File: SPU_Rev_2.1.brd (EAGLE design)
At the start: 127.6 x 101.6 mm, 257 parts, among them Q1 12MHz

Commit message: added LWL IN
added LWL IN
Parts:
- removed C63: 10u, rcl:E/7260-38W
- added C78: (no value), rcl:C1206
- added U$9: PLR135, everlight-fiber-optics-spdif:PLR135-T1
- moved C65 7.11 mm to (91.2, 22.7), turned to 0 degrees
- moved C36 4.72 mm to (100.6, 9.78)
- moved C39 4.57 mm to (91.2, 30.6)
- moved C64 4.45 mm to (91.2, 30.7)
- moved U$8 1.02 mm to (62.0, 16.1)
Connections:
- new net LWL_IN: U$9.VOUT, U_STM32F779.7
- net 3V3: now also C78.1, U$9.VCC
- net 5V: no longer C63.+
- net GND: now also C78.2, U$9.GND; no longer C63.-
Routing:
- net LWL_IN: track 0.00 -> 51.8 mm, vias 0 -> 1
- net 3V3: track 887.6 -> 917.4 mm
- net GND: track 1457.2 -> 1427.5 mm, vias 169 -> 168
- net 5V: track 193.2 -> 197.8 mm
- net 28V: track 219.9 -> 223.9 mm, vias 11 -> 13
- net LWL_OUT: track 37.8 -> 39.0 mm
- net LED_4: track 81.3 -> 82.1 mm

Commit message: Added PT100 ADC R/C values
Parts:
- C_ICM1_PT3, C_ICM2_PT3: value (none) -> 4n7
- C_IDIFF_PT3: value (none) -> 47n
- C_RDIFF_PT3: value (none) -> 100n
- R_I1_PT3, R_I2_PT3: value (none) -> 5k
- R_R1_PT3: value (none) -> 3k16
- R_R2_PT3: value (none) -> inf
- R_REF_PT3: value (none) -> 1k62
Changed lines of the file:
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@@
 <drawing>
 <settings>
-<setting alwaysvectorfont="no"/>
+<setting alwaysvectorfont="yes"/>
 <setting verticaltext="up"/>
 </settings>
@@
 <attribute name="VALUE" x="22.8242" y="84.5312" size="1.016" layer="27" ratio="10" rot="R90"/>
 </element>
-<element name="R_REF_PT3" library="++Bedrahtet" package="R0603" value="" x="25.146" y="87.884" smashed="yes" rot="MR270">
+<element name="R_REF_PT3" library="++Bedrahtet" package="R0603" value="1k62" x="25.146" y="87.884" smashed="yes" rot="MR270">
 <attribute name="NAME" x="30.48" y="89.789" size="1.016" layer="26" font="vector" ratio="15" rot="MR0"/>
 <attribute name="VALUE" x="27.178" y="88.773" size="1.27" layer="28" rot="MR270"/>
 </element>
-<element name="R_R1_PT3" library="++Bedrahtet" package="R0603" value="" x="22.987" y="87.884" smashed="yes" rot="MR270">
+<element name="R_R1_PT3" library="++Bedrahtet" package="R0603" value="3k16" x="22.987" y="87.884" smashed="yes" rot="MR270">
 <attribute name="NAME" x="28.067" y="91.186" size="1.016" layer="26" font="vector" ratio="15" rot="MR0"/>
 <attribute name="VALUE" x="25.019" y="88.773" size="1.27" layer="28" rot="MR270"/>
 </element>
-<element name="R_R2_PT3" library="++Bedrahtet" package="R0603" value="" x="17.272" y="80.264" smashed="yes" rot="MR270">
+<element name="R_R2_PT3" library="++Bedrahtet" package="R0603" value="inf" x="17.272" y="80.264" smashed="yes" rot="MR270">
 <attribute name="NAME" x="16.129" y="81.915" size="1.016" layer="26" font="vector" ratio="15" rot="MR270"/>
 <attribute name="VALUE" x="19.304" y="81.153" size="1.27" layer="28" rot="MR270"/>
 </element>
-<element name="C_RDIFF_PT3" library="rcl" library_urn="urn:adsk.eagle:library:334" package="C0603" package3d_urn="urn:adsk.eagle:package:23616/2" value="" x="17.653" y="86.106" smashed="yes" rot="MR0">
+<element name="C_RDIFF_PT3" library="rcl" library_urn="urn:adsk.eagle:library:334" package="C0603" package3d_urn="urn:adsk.eagle:package:23616/2" value="100n" x="17.653" y="86.106" smashed="yes" rot="MR0">
 <attribute name="NAME" x="14.478" y="88.265" size="1.016" layer="26" font="vector" ratio="15" rot="MR270"/>
 <attribute name="SPICEPREFIX" value="C" x="26.416" y="95.504" size="1.778" layer="28" rot="MR0" display="off"/>
@@
 <attribute name="VALUE" x="15.367" y="80.645" size="1.27" layer="27" rot="R270"/>
 </element>
-<element name="R_I1_PT3" library="++Bedrahtet" package="R0603" value="" x="22.987" y="81.28" smashed="yes" rot="R180">
+<element name="R_I1_PT3" library="++Bedrahtet" package="R0603" value="5k" x="22.987" y="81.28" smashed="yes" rot="R180">
 <attribute name="NAME" x="28.956" y="79.502" size="1.016" layer="25" font="vector" ratio="15" rot="R180"/>
 <attribute name="VALUE" x="23.876" y="83.312" size="1.27" layer="27" rot="R180"/>
 </element>
-<element name="R_I2_PT3" library="++Bedrahtet" package="R0603" value="" x="22.987" y="89.154" smashed="yes" rot="R90">
+<element name="R_I2_PT3" library="++Bedrahtet" package="R0603" value="5k" x="22.987" y="89.154" smashed="yes" rot="R90">
 <attribute name="NAME" x="23.876" y="88.9" size="0.8128" layer="25" font="vector" ratio="15"/>
 <attribute name="VALUE" x="25.019" y="88.265" size="1.27" layer="27" rot="R90"/>
 </element>
-<element name="C_IDIFF_PT3" library="rcl" library_urn="urn:adsk.eagle:library:334" package="C0603" package3d_urn="urn:adsk.eagle:package:23616/2" value="" x="24.003" y="84.328" smashed="yes" rot="R180">
+<element name="C_IDIFF_PT3" library="rcl" library_urn="urn:adsk.eagle:library:334" package="C0603" package3d_urn="urn:adsk.eagle:package:23616/2" value="47n" x="24.003" y="84.328" smashed="yes" rot="R180">
 <attribute name="NAME" x="24.638" y="83.185" size="0.8128" layer="25" font="vector" ratio="15" rot="R180"/>
 <attribute name="SPICEPREFIX" value="C" x="24.003" y="85.852" size="1.778" layer="27" rot="R180" display="off"/>
 <attribute name="VALUE" x="24.638" y="86.233" size="1.27" layer="27" rot="R180"/>
 </element>
-<element name="C_ICM1_PT3" library="rcl" library_urn="urn:adsk.eagle:library:334" package="C0603" package3d_urn="urn:adsk.eagle:package:23616/2" value="" x="20.828" y="80.899" smashed="yes" rot="MR270">
+<element name="C_ICM1_PT3" library="rcl" library_urn="urn:adsk.eagle:library:334" package="C0603" package3d_urn="urn:adsk.eagle:package:23616/2" value="4n7" x="20.828" y="80.899" smashed="yes" rot="MR270">
 <attribute name="NAME" x="19.558" y="82.677" size="1.016" layer="26" font="vector" ratio="15" rot="MR270"/>
 <attribute name="SPICEPREFIX" value="C" x="25.908" y="92.456" size="1.778" layer="28" rot="MR270" display="off"/>
 <attribute name="VALUE" x="22.733" y="81.534" size="1.27" layer="28" rot="MR270"/>
 </element>
-<element name="C_ICM2_PT3" library="rcl" library_urn="urn:adsk.eagle:library:334" package="C0603" package3d_urn="urn:adsk.eagle:package:23616/2" value="" x="24.003" y="86.487" smashed="yes" rot="R180">
+<element name="C_ICM2_PT3" library="rcl" library_urn="urn:adsk.eagle:library:334" package="C0603" package3d_urn="urn:adsk.eagle:package:23616/2" value="4n7" x="24.003" y="86.487" smashed="yes" rot="R180">
 <attribute name="SPICEPREFIX" value="C" x="24.003" y="91.567" size="1.778" layer="27" rot="R180" display="off"/>
 <attribute name="VALUE" x="24.638" y="88.392" size="1.27" layer="27" rot="R180"/>

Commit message: RS422 confirmed
RS422 driver functionality plus optocouplers tested and confirmed
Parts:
- JP_MS, X_PROG: value (none) -> x
- LED7, LED8: value (none) -> 1V9
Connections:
- net PRD_ON renamed PDR_ON
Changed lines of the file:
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@@
 <drawing>
 <settings>
-<setting alwaysvectorfont="yes"/>
+<setting alwaysvectorfont="no"/>
 <setting verticaltext="up"/>
 </settings>
@@
 <attribute name="VALUE" x="66.548" y="12.954" size="1.27" layer="28" rot="MR90"/>
 </element>
-<element name="LED7" library="adafruit" library_urn="urn:adsk.eagle:library:420" package="CHIP-LED0805" package3d_urn="urn:adsk.eagle:package:6240557/1" value="" x="83.439" y="8.255" smashed="yes" rot="R180">
+<element name="LED7" library="adafruit" library_urn="urn:adsk.eagle:library:420" package="CHIP-LED0805" package3d_urn="urn:adsk.eagle:package:6240557/1" value="1V9" x="83.439" y="8.255" smashed="yes" rot="R180">
 <attribute name="NAME" x="83.947" y="9.779" size="1.016" layer="26" font="vector" ratio="15" rot="MR270"/>
 <attribute name="VALUE" x="80.899" y="9.525" size="1.27" layer="27" rot="R270"/>
@@
 <attribute name="VALUE" x="81.026" y="12.954" size="1.27" layer="28" rot="MR90"/>
 </element>
-<element name="LED8" library="adafruit" library_urn="urn:adsk.eagle:library:420" package="CHIP-LED0805" package3d_urn="urn:adsk.eagle:package:6240557/1" value="" x="81.407" y="8.255" smashed="yes" rot="R180">
+<element name="LED8" library="adafruit" library_urn="urn:adsk.eagle:library:420" package="CHIP-LED0805" package3d_urn="urn:adsk.eagle:package:6240557/1" value="1V9" x="81.407" y="8.255" smashed="yes" rot="R180">
 <attribute name="NAME" x="81.915" y="9.779" size="1.016" layer="26" font="vector" ratio="15" rot="MR270"/>
 <attribute name="VALUE" x="78.867" y="9.525" size="1.27" layer="27" rot="R270"/>
@@
 <attribute name="VALUE" x="59.315184375" y="62.405990625" size="1.27" layer="28" rot="MR270"/>
 </element>
-<element name="JP_MS" library="aSparkFun" package="1X02" value="" x="50.504346875" y="65.166596875" smashed="yes" rot="R90">
+<element name="JP_MS" library="aSparkFun" package="1X02" value="x" x="50.504346875" y="65.166596875" smashed="yes" rot="R90">
 <attribute name="NAME" x="47.844453125" y="69.402603125" size="1.016" layer="25" font="vector" ratio="15" rot="R270"/>
 <attribute name="VALUE" x="53.679346875" y="63.896596875" size="1.27" layer="27" rot="R90"/>
@@
 <attribute name="VALUE" x="115.323" y="72.821" size="1.27" layer="28" rot="SMR90"/>
 </element>
-<element name="X_PROG" library="con-lstb" library_urn="urn:adsk.eagle:library:162" package="MA10-2" package3d_urn="urn:adsk.eagle:package:8331/1" value="" x="72.771" y="42.037" smashed="yes" rot="R180">
+<element name="X_PROG" library="con-lstb" library_urn="urn:adsk.eagle:library:162" package="MA10-2" package3d_urn="urn:adsk.eagle:package:8331/1" value="x" x="72.771" y="42.037" smashed="yes" rot="R180">
 <attribute name="MF" value="" x="72.771" y="42.037" size="1.27" layer="27" font="vector" ratio="12" rot="R180" display="off"/>
 <attribute name="MPN" value="" x="72.771" y="42.037" size="1.27" layer="27" font="vector" ratio="12" rot="R180" display="off"/>
@@
 <wire x1="61.989553125" y1="81.90501875" x2="61.951396875" y2="81.943175" width="0.254" layer="1"/>
 </signal>
-<signal name="PRD_ON">
+<signal name="PDR_ON">
 <contactref element="U_STM32F779" pad="203"/>
 <contactref element="R9" pad="1"/>

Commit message: Opto Pull-up adjusted
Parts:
- C77, C78: value (none) -> 100n
- RN12: value 300 -> 1k
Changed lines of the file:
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@@
 <attribute name="VALUE" x="108.204" y="87.605" size="1.27" layer="27" align="top-center"/>
 </element>
-<element name="RN12" library="resistor-dil" library_urn="urn:adsk.eagle:library:342" package="EXBS8V" package3d_urn="urn:adsk.eagle:package:24925/1" value="300" x="108.077" y="87.122" smashed="yes" rot="MR90">
+<element name="RN12" library="resistor-dil" library_urn="urn:adsk.eagle:library:342" package="EXBS8V" package3d_urn="urn:adsk.eagle:package:24925/1" value="1k" x="108.077" y="87.122" smashed="yes" rot="MR90">
 <attribute name="MF" value="" x="108.077" y="87.122" size="1.778" layer="28" rot="MR90" display="off"/>
 <attribute name="MPN" value="" x="108.077" y="87.122" size="1.778" layer="28" rot="MR90" display="off"/>
@@
 <attribute name="NAME" x="61.722" y="9.652" size="1.778" layer="26" rot="MR90"/>
 </element>
-<element name="C77" library="rcl" library_urn="urn:adsk.eagle:library:334" package="C1206" package3d_urn="urn:adsk.eagle:package:23618/2" value="" x="57.658" y="19.685" smashed="yes" rot="MR0">
+<element name="C77" library="rcl" library_urn="urn:adsk.eagle:library:334" package="C1206" package3d_urn="urn:adsk.eagle:package:23618/2" value="100n" x="57.658" y="19.685" smashed="yes" rot="MR0">
 <attribute name="NAME" x="59.182" y="21.082" size="1.27" layer="26" rot="MR0"/>
 <attribute name="SPICEPREFIX" value="C" x="57.658" y="19.685" size="1.778" layer="28" rot="MR0" display="off"/>
@@
 <attribute name="NAME" x="94.996" y="14.351" size="1.778" layer="26" rot="MR90"/>
 </element>
-<element name="C78" library="rcl" library_urn="urn:adsk.eagle:library:334" package="C1206" package3d_urn="urn:adsk.eagle:package:23618/2" value="" x="91.059" y="11.938" smashed="yes" rot="MR270">
+<element name="C78" library="rcl" library_urn="urn:adsk.eagle:library:334" package="C1206" package3d_urn="urn:adsk.eagle:package:23618/2" value="100n" x="91.059" y="11.938" smashed="yes" rot="MR270">
 <attribute name="NAME" x="89.789" y="13.208" size="1.27" layer="26" rot="MR270"/>
 <attribute name="SPICEPREFIX" value="C" x="91.059" y="11.938" size="1.778" layer="28" rot="MR270" display="off"/>

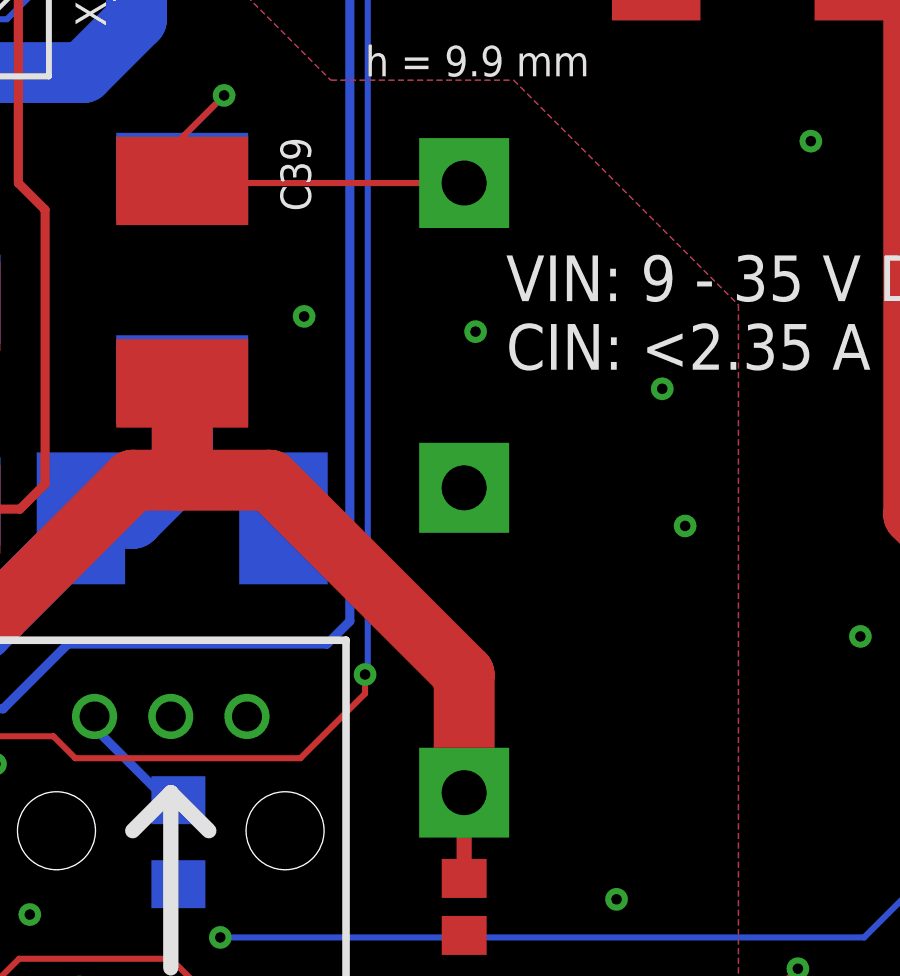
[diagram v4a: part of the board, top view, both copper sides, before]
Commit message: Minor adjustments
adjusted zener values, added optinal trimresistors for voltage setting.
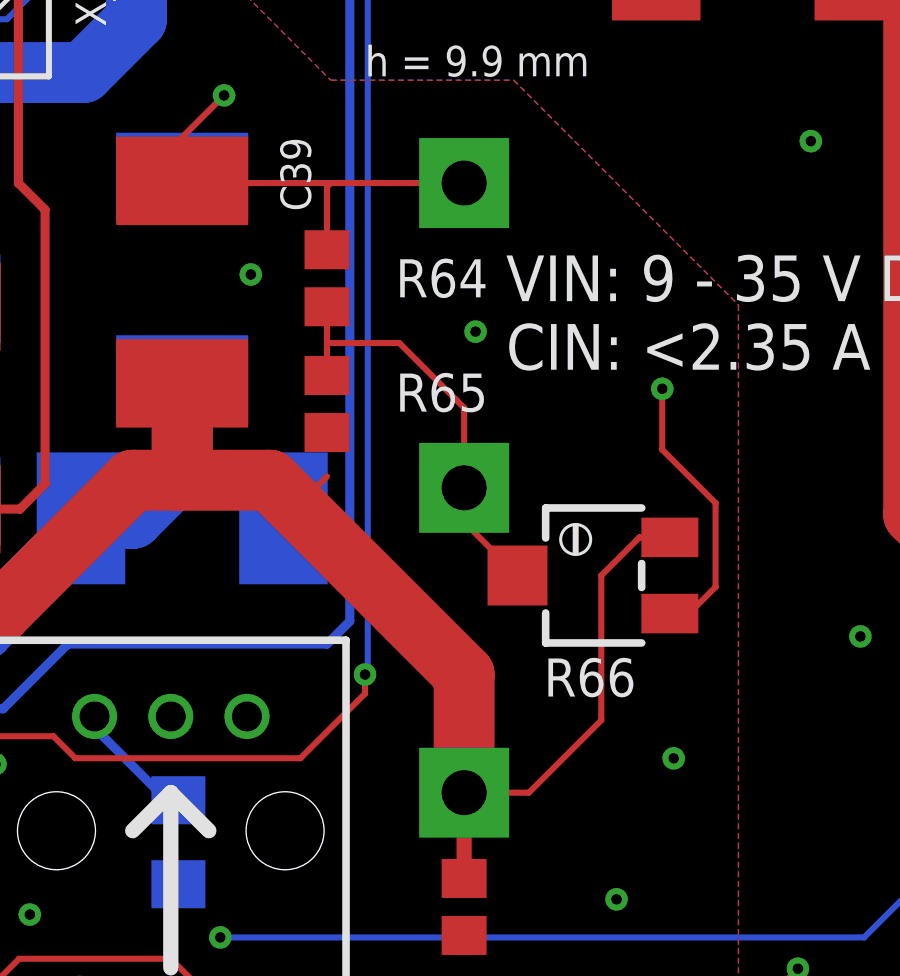
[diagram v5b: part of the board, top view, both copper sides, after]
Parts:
- added R64, R65: inf, rcl:R0805
- added R66: inf, rcl:RTRIM3224X
- D1, D2, D5, D6: value 6V -> 5V6
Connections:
- new net N$17: R64.2, R65.2, R66.2, U_TRACODCDC.4
- net 5V: now also R65.1, R66.3
- net GND: now also R64.1, R66.1
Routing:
- net 5V: track 197.8 -> 212.5 mm
- net N$17: track 0.00 -> 14.1 mm
- net GND: track 1427.5 -> 1439.0 mm
